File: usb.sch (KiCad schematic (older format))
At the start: 15 parts, among them J12 SM05B-SRSS-TB, J16 SM05B-SRSS-TB, J4 SM05B-SRSS-TB, J8 SM05B-SRSS-TB, U1 USB4715, U10 TPS2054BDR

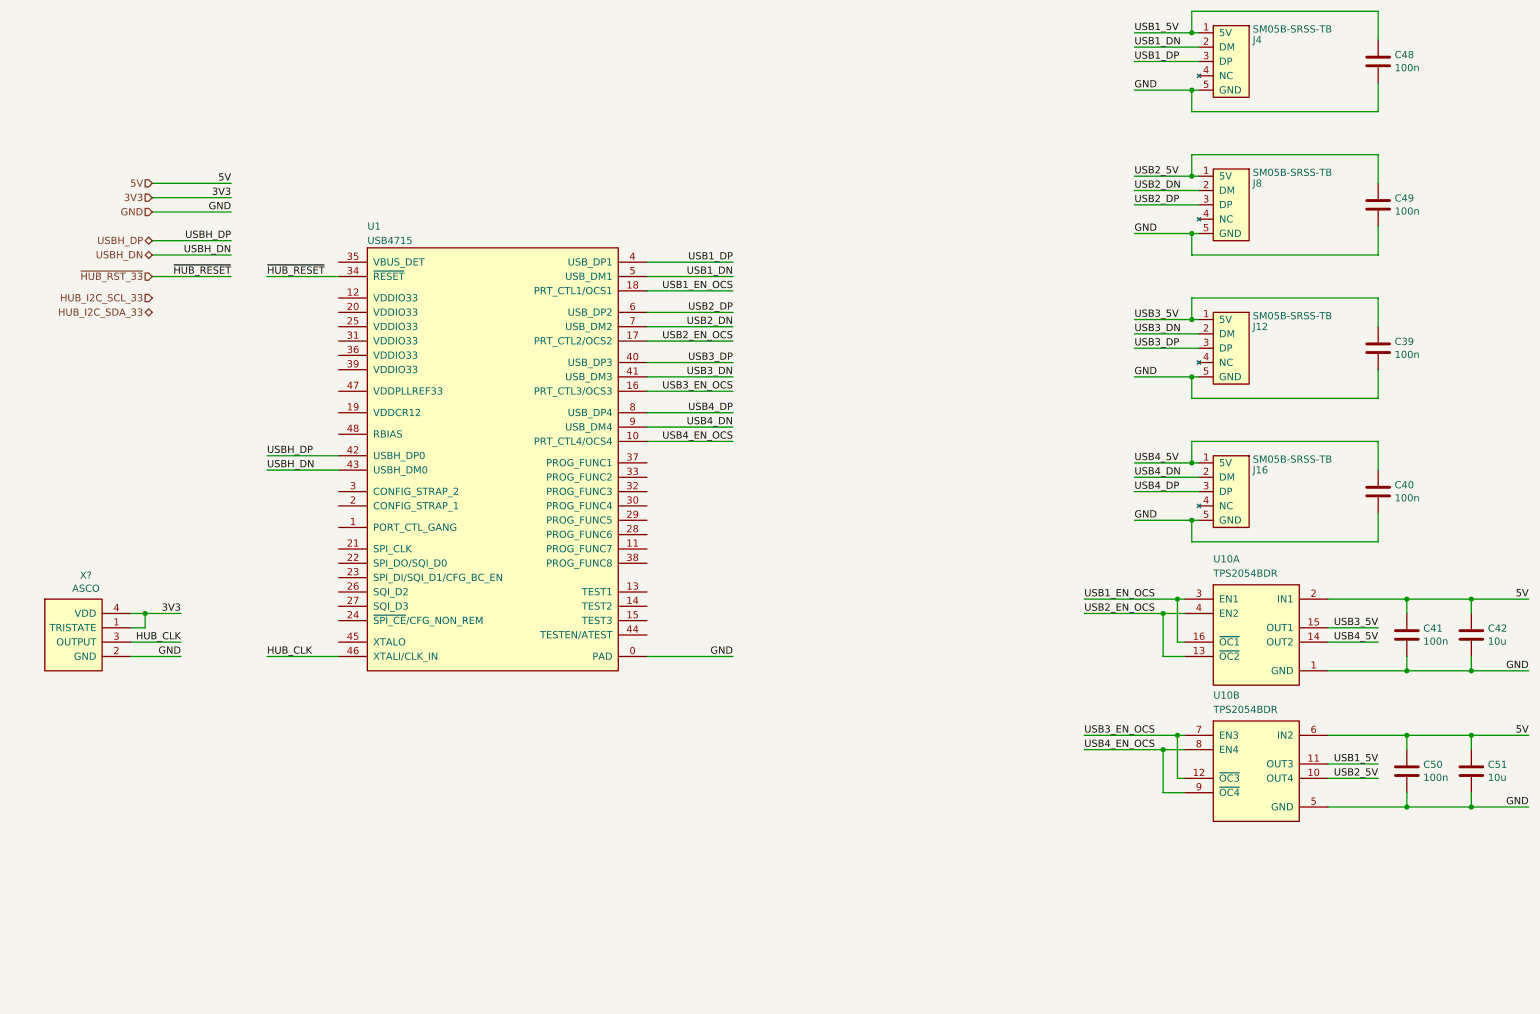
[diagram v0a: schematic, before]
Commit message: Add ferrite bead and POR supervisor for hub
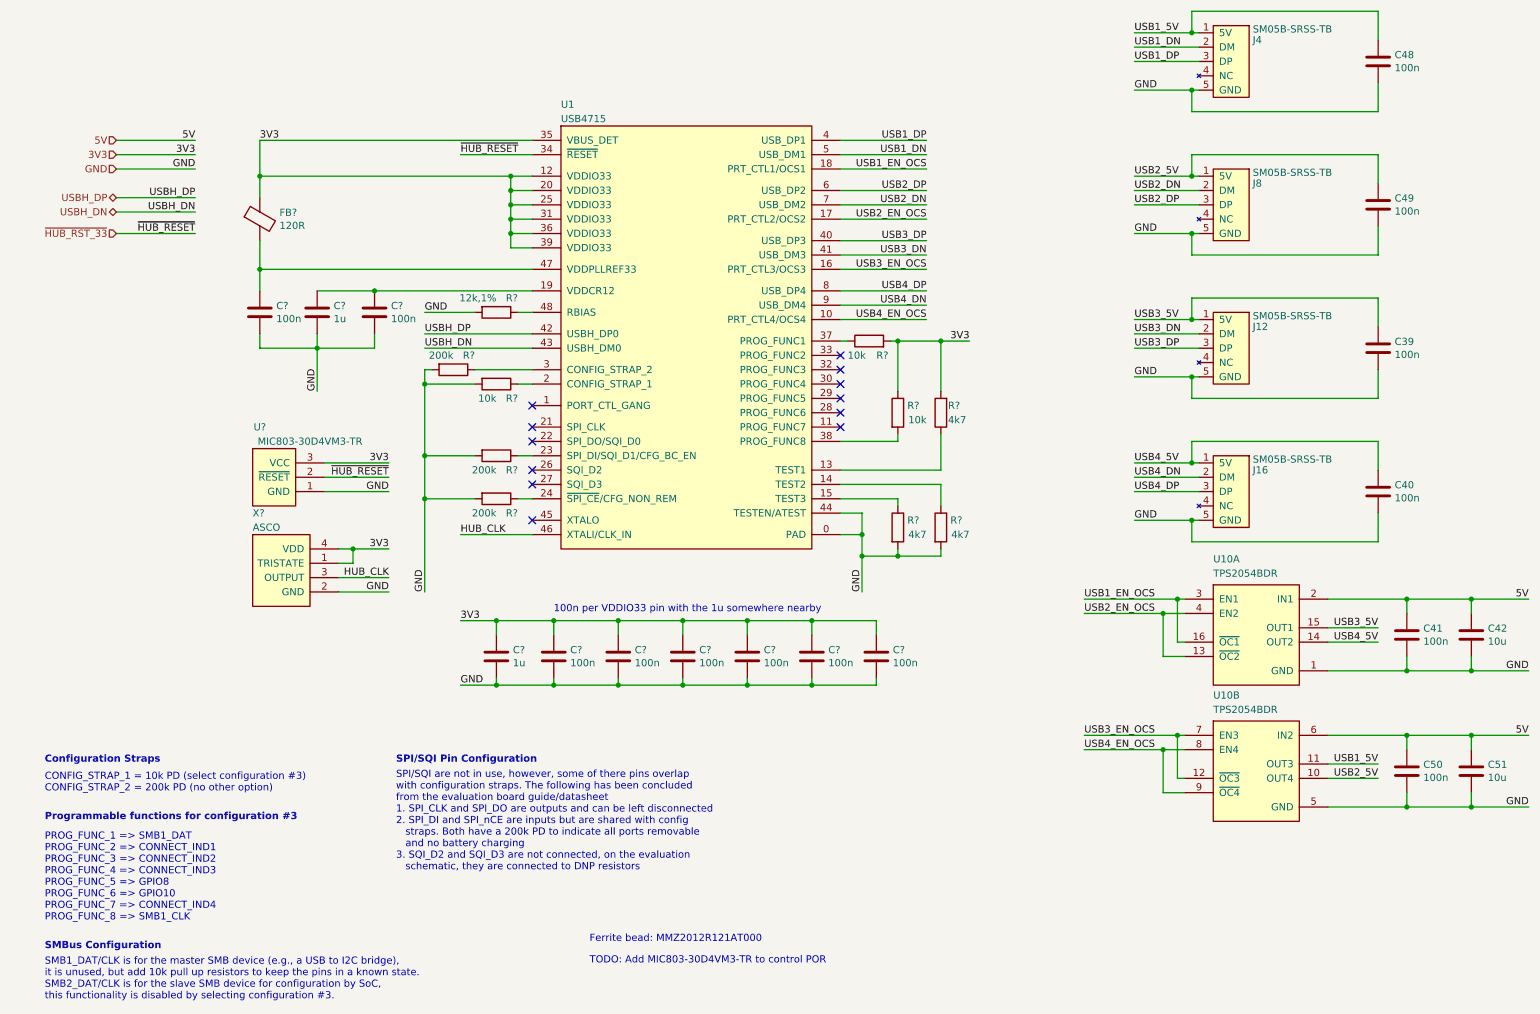
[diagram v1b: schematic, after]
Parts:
- added C? (x8): 100n, Drone:C0805, symbol Drone:CAP
- added C? (x2): 1u, Drone:C0805, symbol Drone:CAP
- added FB?: 120R, Drone:FB0805, symbol Drone:FB
- added R? (x3): 200k, Drone:R0805, symbol Drone:RES
- added R? (x3): 10k, Drone:R0805, symbol Drone:RES
- added R? (x3): 4k7, Drone:R0805, symbol Drone:RES
- added R?: 12k,1%, Drone:R0805, symbol Drone:RES
- added U?: MIC803-30D4VM3-TR, Drone:MIC803-30D4VM3-TR, symbol Drone:MIC803-30D4VM3-TR
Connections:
- net 3V3: now also U1.12 (VDDIO33), U1.20 (VDDIO33), U1.25 (VDDIO33), U1.31 (VDDIO33), U1.35 (VBUS_DET), U1.36 (VDDIO33), U1.39 (VDDIO33), C?.1, C?.1, C?.1, C?.1, C?.1, C?.1, C?.1, FB?.1, R?.1, R?.2, R?.2, U?.3 (VCC)
- net GND: now also U1.44 (TESTEN/ATEST), C?.2, C?.2, C?.2, C?.2, C?.2, C?.2, C?.2, C?.2, C?.2, C?.2, R?.2, R?.2, R?.2, R?.2, R?.2, R?.2, R?.2, U?.1 (GND)
- net ~HUB_RST_33: now also U?.2 (~RESET)
- net at U1.13 (TEST1): now also R?.1
- net at U1.14 (TEST2): now also R?.1
- net at U1.15 (TEST3): now also R?.1
- net at U1.19 (VDDCR12): now also C?.1, C?.1
- net at U1.2 (CONFIG_STRAP_1): now also R?.1
- net at U1.23 (SPI_DI/SQI_D1/CFG_BC_EN): now also R?.1
- net at U1.24 (~SPI_CE~/CFG_NON_REM): now also R?.1
- net at U1.3 (CONFIG_STRAP_2): now also R?.1
- net at U1.37 (PROG_FUNC1): now also R?.1
- net at U1.38 (PROG_FUNC8): now also R?.2
- net at U1.47 (VDDPLLREF33): now also C?.1, FB?.2
- net at U1.48 (RBIAS): now also R?.1
- no-connect marks 0 -> 12
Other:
- note added: "100n per VDDIO33 pin with the 1u somewhere nearby"
- note added: "CONFIG_STRAP_1 = 10k PD (select configuration #3)\nCONFIG_STRAP_2 = 200k PD (no other option)"
- note added: "Configuration Straps"
- note added: "Ferrite bead: MMZ2012R121AT000"
- note added: "PROG_FUNC_1 => SMB1_DAT\nPROG_FUNC_2 => CONNECT_IND1\nPROG_FUNC_3 => CONNECT_IND2\nPROG_FUNC_4 => CONNECT_IND3\nPROG_FUNC_5 => GPIO8\nPROG_FUNC_6 => GPIO10\nPROG_FUNC_7 => CONNECT_IND4\nPROG_FUNC_8 => SMB1_CLK"
- note added: "Programmable functions for configuration #3"
- note added: "SMB1_DAT/CLK is for the master SMB device (e.g., a USB to I2C bridge),\nit is unused, but add 10k pull up resistors to keep the pins in a known state.\nSMB2_DAT/CLK is for the slave SMB device for configuration by SoC,\nthis functionality is disabled by selecting configuration #3."
- note added: "SMBus Configuration"
- note added: "SPI/SQI Pin Configuration"
- note added: "SPI/SQI are not in use, however, some of there pins overlap\nwith configuration straps. The following has been concluded\nfrom the evaluation board guide/datasheet\n1. SPI_CLK and SPI_DO are outputs and can be left disconnected\n2. SPI_DI and SPI_nCE are inputs but are shared with config\n straps. Both have a 200k PD to indicate all ports removable\n and no battery charging\n3. SQI_D2 and SQI_D3 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"
- note added: "TODO: Add MIC803-30D4VM3-TR to control POR"
- moved on the sheet: U1, X?

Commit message: Replace old components and related tracks, vias, etc on PCB with new components.
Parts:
- gave numbers to parts that had none: 23
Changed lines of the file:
@@
 USBH_DN
 $Comp
-L Drone:ASCO X?
+L Drone:ASCO X1
 U 1 1 60A75D06
 P 2150 4350
-F 0 "X?" H 2150 4500 50  0000 L CNN
+F 0 "X1" H 2150 4500 50  0000 L CNN
 F 1 "ASCO" H 2150 4400 50  0000 L CNN
 F 2 "Drone:ASCO" H 2150 3800 50  0001 L CNN
@@
 Programmable functions for configuration #3
 $Comp
-L Drone:RES R?
+L Drone:RES R37
 U 1 1 609A8356
 P 3550 3200
-AR Path="/5E2EDC4D/609A8356" Ref="R?"  Part="1"
+AR Path="/5E2EDC4D/609A8356" Ref="R37"  Part="1"
 AR Path="/609A8356" Ref="R?"  Part="1"
-F 0 "R?" V 3450 3350 50  0000 R CNN
+F 0 "R37" V 3450 3350 50  0000 R CNN
 F 1 "200k" V 3450 3200 50  0000 R CNN
 F 2 "Drone:R0805" V 3480 3200 50  0001 C CNN
@@
 SMB1_DAT/CLK is for the master SMB device (e.g., a USB to I2C bridge),\nit is unused, but add 10k pull up resistors to keep the pins in a known state.\nSMB2_DAT/CLK is for the slave SMB device for configuration by SoC,\nthis functionality is disabled by selecting configuration #3.
 $Comp
-L Drone:RES R?
+L Drone:RES R44
 U 1 1 609FB2E7
 P 6650 3500
-AR Path="/5E2EDC4D/609FB2E7" Ref="R?"  Part="1"
+AR Path="/5E2EDC4D/609FB2E7" Ref="R44"  Part="1"
 AR Path="/609FB2E7" Ref="R?"  Part="1"
-F 0 "R?" H 6800 3550 50  0000 R CNN
+F 0 "R44" H 6800 3550 50  0000 R CNN
 F 1 "10k" H 6850 3450 50  0000 R CNN
 F 2 "Drone:R0805" V 6580 3500 50  0001 C CNN
@@
 $EndComp
 $Comp
-L Drone:RES R?
+L Drone:RES R43
 U 1 1 609FC448
 P 6450 3000
-AR Path="/5E2EDC4D/609FC448" Ref="R?"  Part="1"
+AR Path="/5E2EDC4D/609FC448" Ref="R43"  Part="1"
 AR Path="/609FC448" Ref="R?"  Part="1"
-F 0 "R?" V 6350 2950 50  0000 R CNN
+F 0 "R43" V 6350 2950 50  0000 R CNN
 F 1 "10k" V 6350 3150 50  0000 R CNN
 F 2 "Drone:R0805" V 6380 3000 50  0001 C CNN
@@
 	6250 4350 6400 4350
 $Comp
-L Drone:RES R?
+L Drone:RES R83
 U 1 1 60A6AD36
 P 6950 3500
-AR Path="/5E2EDC4D/60A6AD36" Ref="R?"  Part="1"
+AR Path="/5E2EDC4D/60A6AD36" Ref="R83"  Part="1"
 AR Path="/60A6AD36" Ref="R?"  Part="1"
-F 0 "R?" H 6900 3450 50  0000 R CNN
+F 0 "R83" H 6900 3450 50  0000 R CNN
 F 1 "4k7" H 6900 3550 50  0000 R CNN
 F 2 "Drone:R0805" V 6880 3500 50  0001 C CNN
@@
 $EndComp
 $Comp
-L Drone:RES R?
+L Drone:RES R82
 U 1 1 60A6B095
 P 6650 4300
-AR Path="/5E2EDC4D/60A6B095" Ref="R?"  Part="1"
+AR Path="/5E2EDC4D/60A6B095" Ref="R82"  Part="1"
 AR Path="/60A6B095" Ref="R?"  Part="1"
-F 0 "R?" H 6800 4350 50  0000 R CNN
+F 0 "R82" H 6800 4350 50  0000 R CNN
 F 1 "4k7" H 6850 4250 50  0000 R CNN
 F 2 "Drone:R0805" V 6580 4300 50  0001 C CNN
@@
 	6950 3000 7150 3000
 $Comp
-L Drone:RES R?
+L Drone:RES R84
 U 1 1 60B5867F
 P 6950 4300
-AR Path="/5E2EDC4D/60B5867F" Ref="R?"  Part="1"
+AR Path="/5E2EDC4D/60B5867F" Ref="R84"  Part="1"
 AR Path="/60B5867F" Ref="R?"  Part="1"
-F 0 "R?" H 7100 4350 50  0000 R CNN
+F 0 "R84" H 7100 4350 50  0000 R CNN
 F 1 "4k7" H 7150 4250 50  0000 R CNN
 F 2 "Drone:R0805" V 6880 4300 50  0001 C CNN
@@
 NoConn ~ 4100 4000
 $Comp
-L Drone:RES R?
+L Drone:RES R41
 U 1 1 60C216A6
 P 3850 3800
-AR Path="/5E2EDC4D/60C216A6" Ref="R?"  Part="1"
+AR Path="/5E2EDC4D/60C216A6" Ref="R41"  Part="1"
 AR Path="/60C216A6" Ref="R?"  Part="1"
-F 0 "R?" V 3950 3950 50  0000 R CNN
+F 0 "R41" V 3950 3950 50  0000 R CNN
 F 1 "200k" V 3950 3800 50  0000 R CNN
 F 2 "Drone:R0805" V 3780 3800 50  0001 C CNN
@@
 	3700 3800 3350 3800
 $Comp
-L Drone:RES R?
+L Drone:RES R42
 U 1 1 60C3D45B
 P 3850 4100
-AR Path="/5E2EDC4D/60C3D45B" Ref="R?"  Part="1"
+AR Path="/5E2EDC4D/60C3D45B" Ref="R42"  Part="1"
 AR Path="/60C3D45B" Ref="R?"  Part="1"
-F 0 "R?" V 3950 4250 50  0000 R CNN
+F 0 "R42" V 3950 4250 50  0000 R CNN
 F 1 "200k" V 3950 4100 50  0000 R CNN
 F 2 "Drone:R0805" V 3780 4100 50  0001 C CNN
@@
 	3700 4100 3350 4100
 $Comp
-L Drone:RES R?
+L Drone:RES R40
 U 1 1 60C4FD75
 P 3850 3300
-AR Path="/5E2EDC4D/60C4FD75" Ref="R?"  Part="1"
+AR Path="/5E2EDC4D/60C4FD75" Ref="R40"  Part="1"
 AR Path="/60C4FD75" Ref="R?"  Part="1"
-F 0 "R?" V 3950 3450 50  0000 R CNN
+F 0 "R40" V 3950 3450 50  0000 R CNN
 F 1 "10k" V 3950 3300 50  0000 R CNN
 F 2 "Drone:R0805" V 3780 3300 50  0001 C CNN
@@
 	3350 4100 3350 4750
 $Comp
-L Drone:RES R?
+L Drone:RES R39
 U 1 1 60CF3062
 P 3850 2800
-AR Path="/5E2EDC4D/60CF3062" Ref="R?"  Part="1"
+AR Path="/5E2EDC4D/60CF3062" Ref="R39"  Part="1"
 AR Path="/60CF3062" Ref="R?"  Part="1"
-F 0 "R?" V 3750 2950 50  0000 R CNN
+F 0 "R39" V 3750 2950 50  0000 R CNN
 F 1 "12k,1%" V 3750 2800 50  0000 R CNN
 F 2 "Drone:R0805" V 3780 2800 50  0001 C CNN
@@
 Ferrite bead: MMZ2012R121AT000
 $Comp
-L Drone:CAP C?
+L Drone:CAP C37
 U 1 1 60D2CB83
 P 4250 5200
-AR Path="/5E2EDC4D/60D2CB83" Ref="C?"  Part="1"
+AR Path="/5E2EDC4D/60D2CB83" Ref="C37"  Part="1"
 AR Path="/5E349830/60D2CB83" Ref="C?"  Part="1"
-F 0 "C?" H 4365 5246 50  0000 L CNN
+F 0 "C37" H 4365 5246 50  0000 L CNN
 F 1 "100n" H 4365 5155 50  0000 L CNN
 F 2 "Drone:C0805" H 4288 5050 50  0001 C CNN
@@
 $EndComp
 $Comp
-L Drone:CAP C?
+L Drone:CAP C38
 U 1 1 60D30725
 P 4700 5200
-AR Path="/5E2EDC4D/60D30725" Ref="C?"  Part="1"
+AR Path="/5E2EDC4D/60D30725" Ref="C38"  Part="1"
 AR Path="/5E349830/60D30725" Ref="C?"  Part="1"
-F 0 "C?" H 4815 5246 50  0000 L CNN
+F 0 "C38" H 4815 5246 50  0000 L CNN
 F 1 "100n" H 4815 5155 50  0000 L CNN
 F 2 "Drone:C0805" H 4738 5050 50  0001 C CNN
@@
 $EndComp
 $Comp
-L Drone:CAP C?
+L Drone:CAP C43
 U 1 1 60D32218
 P 5150 5200
-AR Path="/5E2EDC4D/60D32218" Ref="C?"  Part="1"
+AR Path="/5E2EDC4D/60D32218" Ref="C43"  Part="1"
 AR Path="/5E349830/60D32218" Ref="C?"  Part="1"
-F 0 "C?" H 5265 5246 50  0000 L CNN
+F 0 "C43" H 5265 5246 50  0000 L CNN
 F 1 "100n" H 5265 5155 50  0000 L CNN
 F 2 "Drone:C0805" H 5188 5050 50  0001 C CNN
@@
 $EndComp
 $Comp
-L Drone:CAP C?
+L Drone:CAP C44
 U 1 1 60D3266E
 P 5600 5200
-AR Path="/5E2EDC4D/60D3266E" Ref="C?"  Part="1"
+AR Path="/5E2EDC4D/60D3266E" Ref="C44"  Part="1"
 AR Path="/5E349830/60D3266E" Ref="C?"  Part="1"
-F 0 "C?" H 5715 5246 50  0000 L CNN
+F 0 "C44" H 5715 5246 50  0000 L CNN
 F 1 "100n" H 5715 5155 50  0000 L CNN
 F 2 "Drone:C0805" H 5638 5050 50  0001 C CNN
@@
 $EndComp
 $Comp
-L Drone:CAP C?
+L Drone:CAP C45
 U 1 1 60D32C93
 P 6050 5200
-AR Path="/5E2EDC4D/60D32C93" Ref="C?"  Part="1"
+AR Path="/5E2EDC4D/60D32C93" Ref="C45"  Part="1"
 AR Path="/5E349830/60D32C93" Ref="C?"  Part="1"
-F 0 "C?" H 6165 5246 50  0000 L CNN
+F 0 "C45" H 6165 5246 50  0000 L CNN
 F 1 "100n" H 6165 5155 50  0000 L CNN
 F 2 "Drone:C0805" H 6088 5050 50  0001 C CNN
@@
 $EndComp
 $Comp
-L Drone:CAP C?
+L Drone:CAP C46
 U 1 1 60D32FEE
 P 6500 5200
-AR Path="/5E2EDC4D/60D32FEE" Ref="C?"  Part="1"
+AR Path="/5E2EDC4D/60D32FEE" Ref="C46"  Part="1"
 AR Path="/5E349830/60D32FEE" Ref="C?"  Part="1"
-F 0 "C?" H 6615 5246 50  0000 L CNN
+F 0 "C46" H 6615 5246 50  0000 L CNN
 F 1 "100n" H 6615 5155 50  0000 L CNN
 F 2 "Drone:C0805" H 6538 5050 50  0001 C CNN
@@
 	4250 5400 4700 5400
 $Comp
-L Drone:CAP C?
+L Drone:CAP C36
 U 1 1 60D50E4B
 P 3850 5200
-AR Path="/5E2EDC4D/60D50E4B" Ref="C?"  Part="1"
+AR Path="/5E2EDC4D/60D50E4B" Ref="C36"  Part="1"
 AR Path="/5E349830/60D50E4B" Ref="C?"  Part="1"
-F 0 "C?" H 3965 5246 50  0000 L CNN
+F 0 "C36" H 3965 5246 50  0000 L CNN
 F 1 "1u" H 3965 5155 50  0000 L CNN
 F 2 "Drone:C0805" H 3888 5050 50  0001 C CNN
@@
 Connection ~ 3850 5400
 $Comp
-L Drone:FB FB?
+L Drone:FB FB1
 U 1 1 60A016FF
 P 2200 2150
-F 0 "FB?" H 2337 2196 50  0000 L CNN
+F 0 "FB1" H 2337 2196 50  0000 L CNN
 F 1 "120R" H 2337 2105 50  0000 L CNN
 F 2 "Drone:FB0805" V 1950 2150 50  0001 C CNN
@@
 $EndComp
 $Comp
-L Drone:CAP C?
+L Drone:CAP C35
 U 1 1 60A29381
 P 3000 2800
-AR Path="/5E2EDC4D/60A29381" Ref="C?"  Part="1"
+AR Path="/5E2EDC4D/60A29381" Ref="C35"  Part="1"
 AR Path="/5E349830/60A29381" Ref="C?"  Part="1"
-F 0 "C?" H 3115 2846 50  0000 L CNN
+F 0 "C35" H 3115 2846 50  0000 L CNN
 F 1 "100n" H 3115 2755 50  0000 L CNN
 F 2 "Drone:C0805" H 3038 2650 50  0001 C CNN
@@
 $EndComp
 $Comp
-L Drone:CAP C?
+L Drone:CAP C34
 U 1 1 60A64B99
 P 2600 2800
-AR Path="/5E2EDC4D/60A64B99" Ref="C?"  Part="1"
+AR Path="/5E2EDC4D/60A64B99" Ref="C34"  Part="1"
 AR Path="/5E349830/60A64B99" Ref="C?"  Part="1"
-F 0 "C?" H 2715 2846 50  0000 L CNN
+F 0 "C34" H 2715 2846 50  0000 L CNN
 F 1 "1u" H 2715 2755 50  0000 L CNN
 F 2 "Drone:C0805" H 2638 2650 50  0001 C CNN
@@
 	3000 2650 4100 2650
 $Comp
-L Drone:CAP C?
+L Drone:CAP C1
 U 1 1 60A7F86A
 P 2200 2800
-AR Path="/5E2EDC4D/60A7F86A" Ref="C?"  Part="1"
+AR Path="/5E2EDC4D/60A7F86A" Ref="C1"  Part="1"
 AR Path="/5E349830/60A7F86A" Ref="C?"  Part="1"
-F 0 "C?" H 2315 2846 50  0000 L CNN
+F 0 "C1" H 2315 2846 50  0000 L CNN
 F 1 "100n" H 2315 2755 50  0000 L CNN
 F 2 "Drone:C0805" H 2238 2650 50  0001 C CNN
@@
 3V3
 $Comp
-L Drone:MIC803-30D4VM3-TR U?
+L Drone:MIC803-30D4VM3-TR U9
 U 1 1 60BCAC18
 P 2150 3750
-F 0 "U?" H 2200 3900 50  0000 C CNN
+F 0 "U9" H 2200 3900 50  0000 C CNN
 F 1 "MIC803-30D4VM3-TR" H 2550 3800 50  0000 C CNN
 F 2 "Drone:MIC803-30D4VM3-TR" H 2150 3300 50  0001 L CNN
